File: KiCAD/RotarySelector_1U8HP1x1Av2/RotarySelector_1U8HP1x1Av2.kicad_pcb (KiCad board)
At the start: 2 copper layers, 40.3 x 39.7 mm, 5 parts

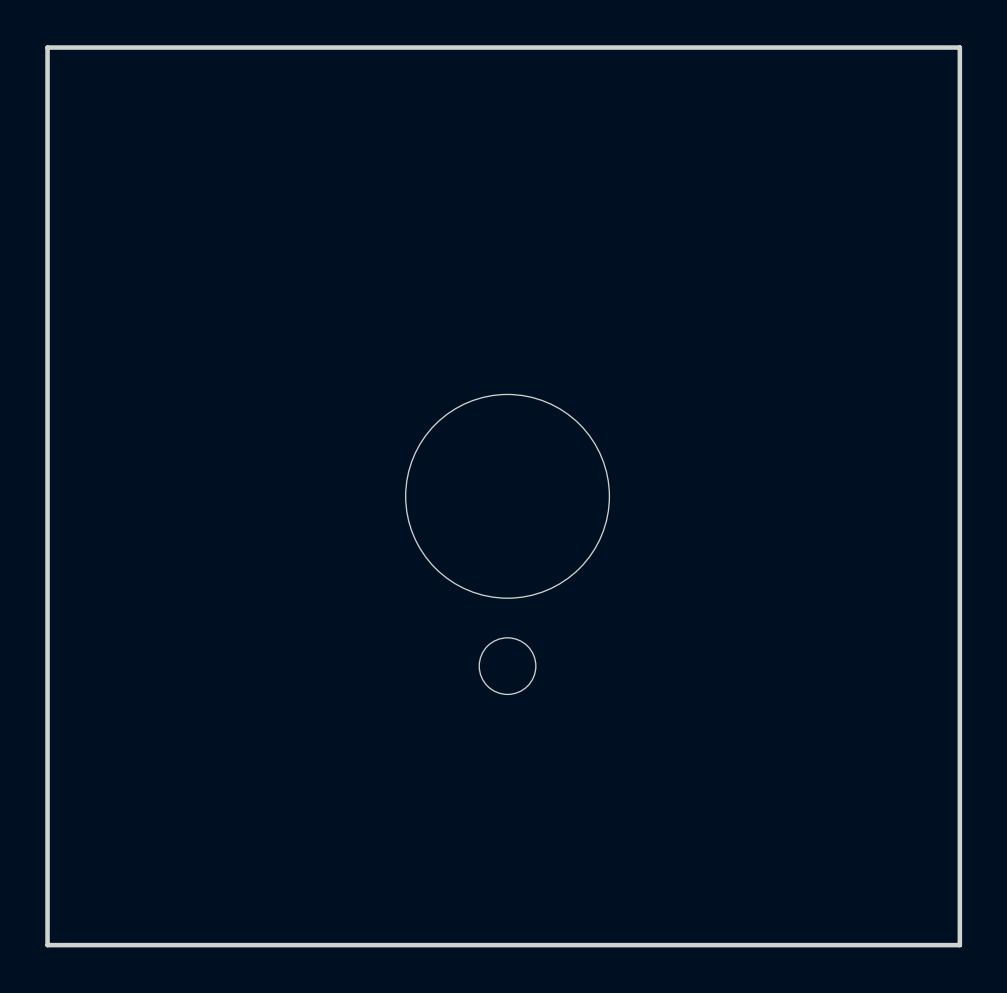
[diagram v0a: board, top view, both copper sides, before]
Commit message: updated all modules to use plated through-holes wherever possible
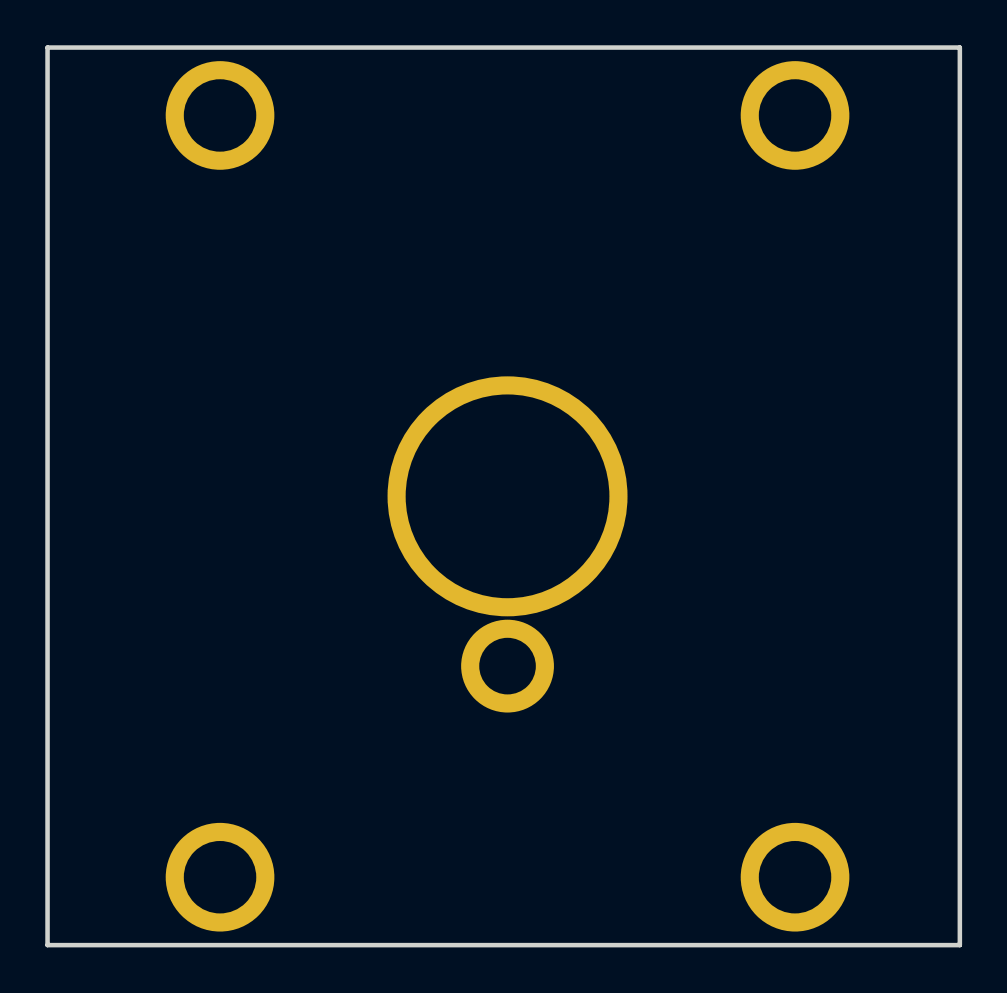
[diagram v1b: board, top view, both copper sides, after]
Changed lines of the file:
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@@
 			)
 		)
-		(pad "" np_thru_hole oval
+		(pad "" thru_hole circle
 			(at 0 0)
-			(size 4.34 3.2)
-			(drill oval 4.34 3.2)
-			(layers "*.Cu" "*.Mask")
+			(size 4.8 4.8)
+			(drill 3.2)
+			(layers "*.Cu" "*.Mask")
+			(remove_unused_layers no)
 		)
 		(embedded_fonts no)
@@
 			)
 		)
-		(pad "" np_thru_hole oval
+		(pad "" thru_hole circle
 			(at 0 0)
-			(size 4.34 3.2)
-			(drill oval 4.34 3.2)
-			(layers "*.Cu" "*.Mask")
+			(size 4.8 4.8)
+			(drill 3.2)
+			(layers "*.Cu" "*.Mask")
+			(remove_unused_layers no)
 		)
 		(embedded_fonts no)
@@
 			)
 		)
-		(pad "" np_thru_hole oval
+		(pad "" thru_hole circle
 			(at 0 0)
-			(size 4.34 3.2)
-			(drill oval 4.34 3.2)
-			(layers "*.Cu" "*.Mask")
+			(size 4.8 4.8)
+			(drill 3.2)
+			(layers "*.Cu" "*.Mask")
+			(remove_unused_layers no)
 		)
 		(embedded_fonts no)
@@
 			)
 		)
-		(pad "" np_thru_hole oval
+		(pad "" thru_hole circle
 			(at 0 0)
-			(size 4.34 3.2)
-			(drill oval 4.34 3.2)
-			(layers "*.Cu" "*.Mask")
+			(size 4.8 4.8)
+			(drill 3.2)
+			(layers "*.Cu" "*.Mask")
+			(remove_unused_layers no)
 		)
 		(embedded_fonts no)
@@
 			)
 		)
-		(pad "" np_thru_hole circle
+		(pad "" thru_hole circle
 			(at 0 0)
-			(size 9 9)
+			(size 10.6 10.6)
 			(drill 9)
 			(layers "*.Cu" "*.Mask")
-		)
-		(pad "" np_thru_hole circle
+			(remove_unused_layers no)
+		)
+		(pad "" thru_hole circle
 			(at 0 7.5)
-			(size 2.5 2.5)
+			(size 4.1 4.1)
 			(drill 2.5)
 			(layers "*.Cu" "*.Mask")
+			(remove_unused_layers no)
 		)
 		(embedded_fonts no)
